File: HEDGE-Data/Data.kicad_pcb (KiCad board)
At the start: 2 copper layers, 90.2 x 95.9 mm, 6 parts

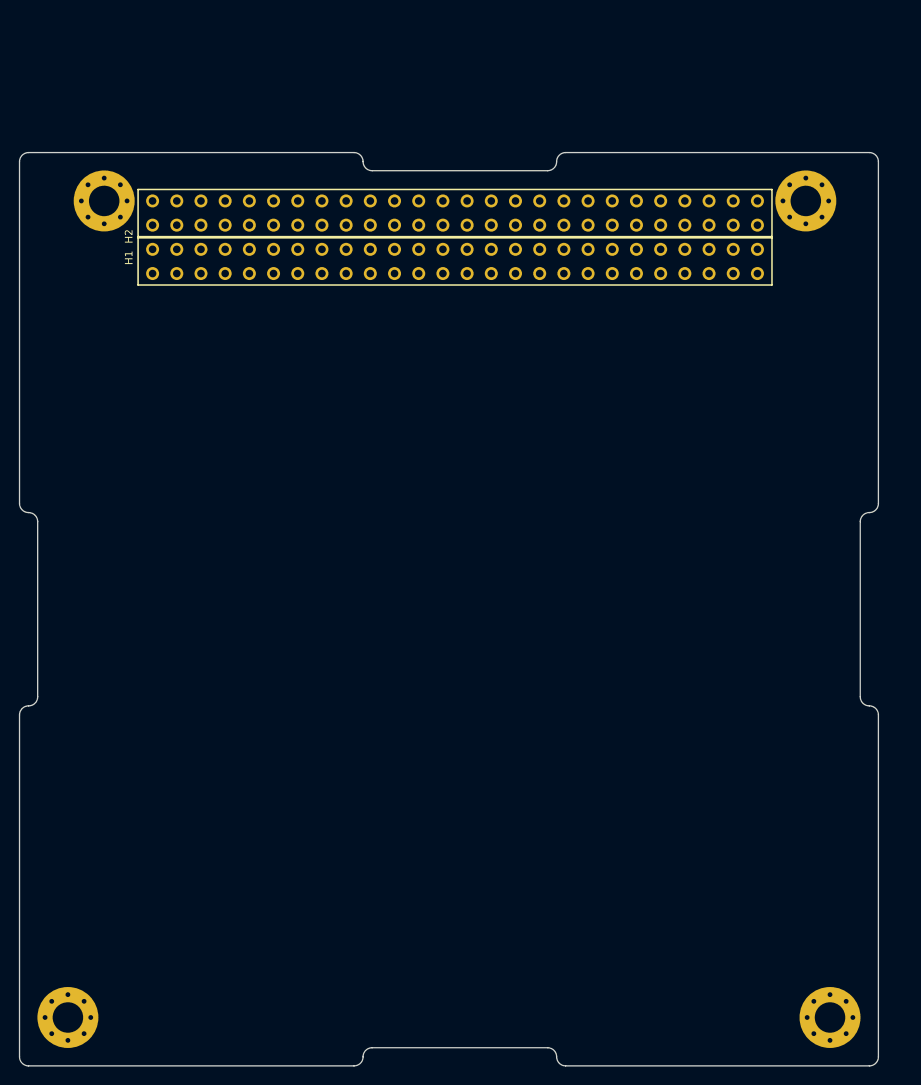
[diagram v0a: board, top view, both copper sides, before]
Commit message: Refactor Data PCB files; enter RS485; enter Iridium radio power
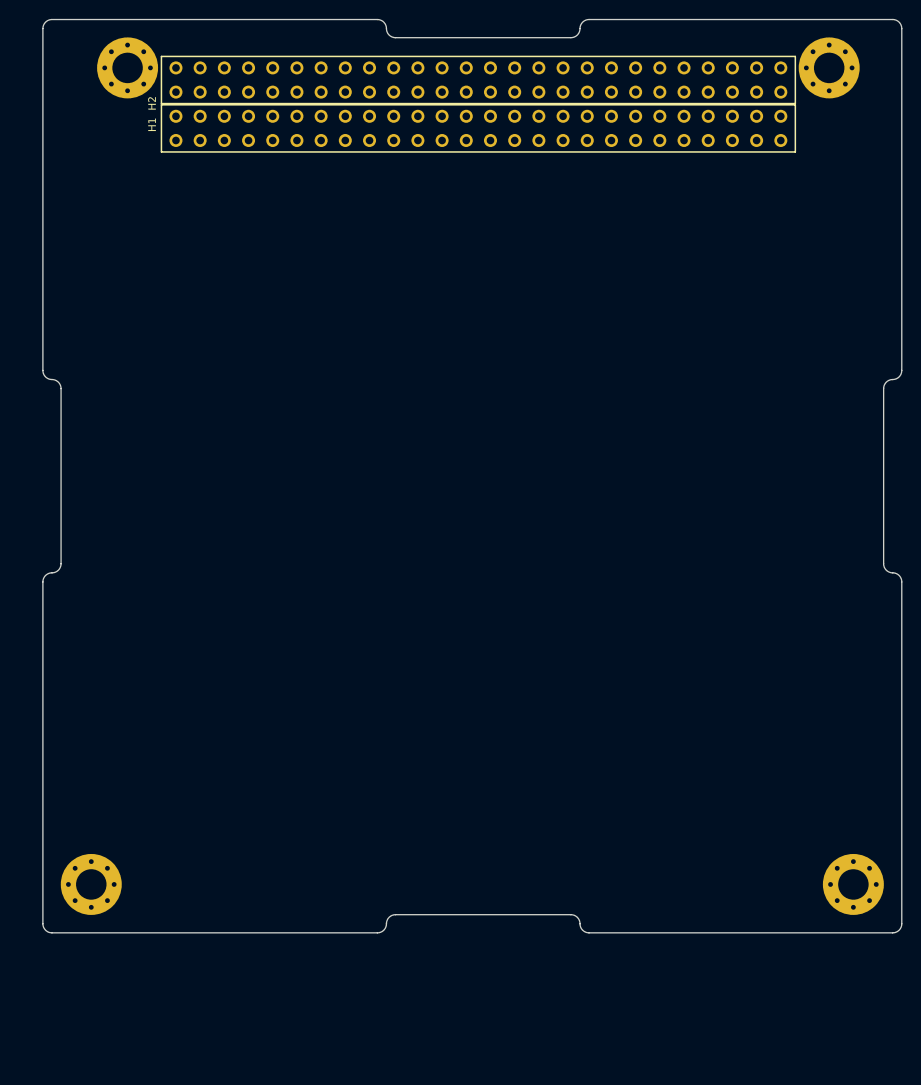
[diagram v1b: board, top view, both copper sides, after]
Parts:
- moved MH3 14.2 mm to (192.3, 134.4)
- moved MH4 14.2 mm to (112.3, 134.4)
- moved H1 14.2 mm to (121.2, 56.3)
- moved H2 14.2 mm to (121.2, 51.2)
- moved MH1 14.2 mm to (116.1, 48.7)
- moved MH2 14.2 mm to (189.8, 48.7)
